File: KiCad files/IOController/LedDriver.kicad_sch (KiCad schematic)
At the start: 28 parts, among them IC1 TPS922054DMTR

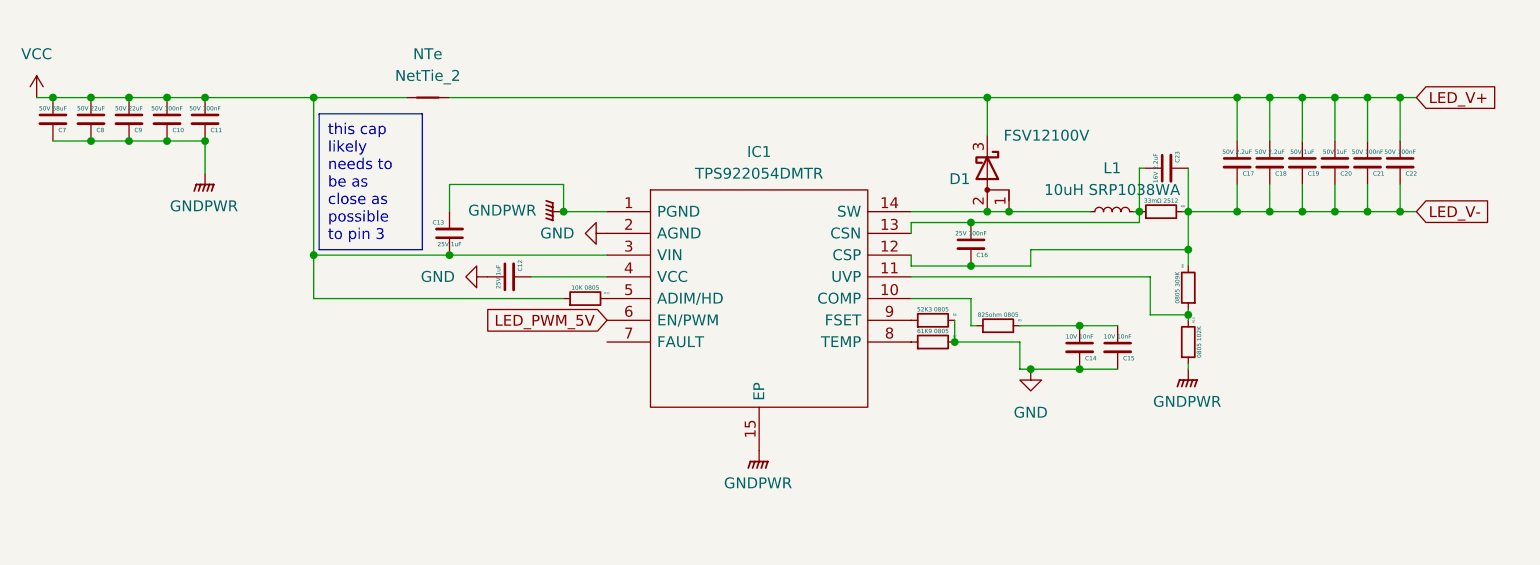
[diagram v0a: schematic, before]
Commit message: started re-work of led driver circuit on IO board
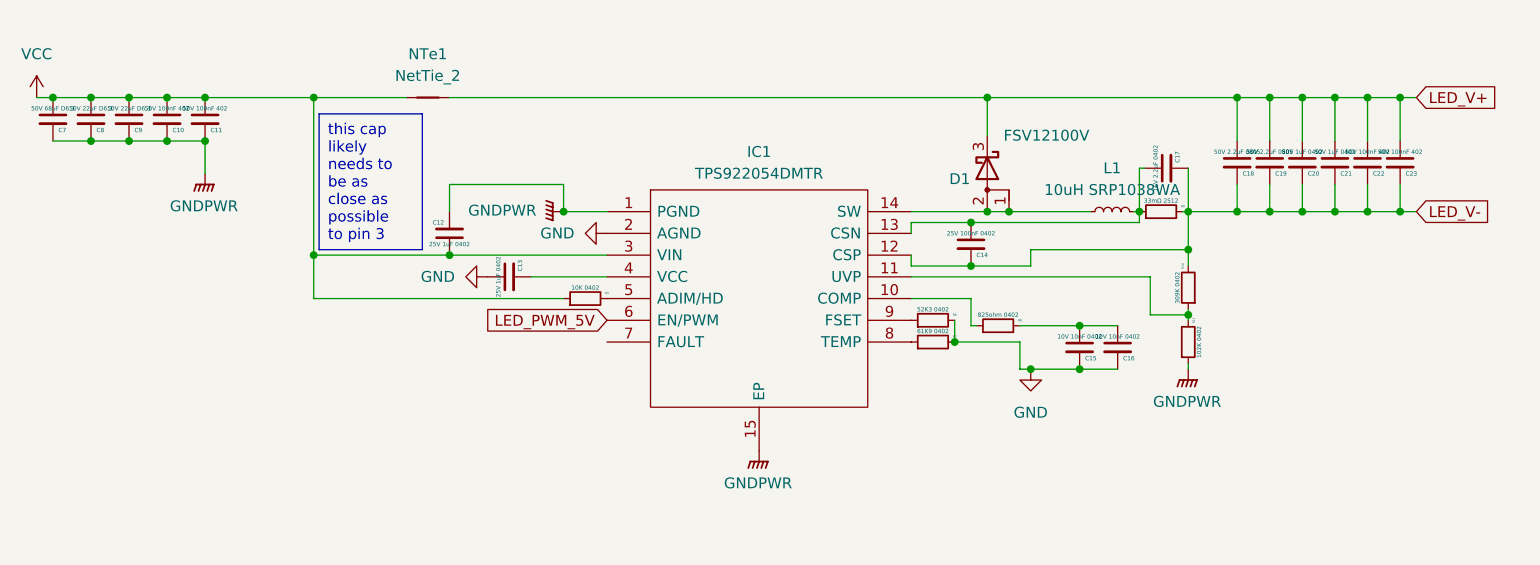
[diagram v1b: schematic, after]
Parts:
- C10, C11: value 50V 100nF -> 50V 100nF 402; footprint Capacitor_SMD:CP_Elec_8x5.4 -> Capacitor_SMD:C_0402_1005Metric
- C12: renamed from C13; value 25V 1uF -> 25V 1uF 0402; footprint Capacitor_SMD:CP_Elec_8x5.4 -> Capacitor_SMD:C_0402_1005Metric
- C13: renamed from C12; value 25V 1uF -> 25V 1uF 0402; footprint Capacitor_SMD:CP_Elec_8x5.4 -> Capacitor_SMD:C_0402_1005Metric
- C14: renamed from C16; value 25V 100nF -> 25V 100nF 0402; footprint Capacitor_SMD:CP_Elec_8x5.4 -> Capacitor_SMD:C_0402_1005Metric
- C15: renamed from C14; value 10V 10nF -> 10V 10nF 0402; footprint Capacitor_SMD:CP_Elec_8x5.4 -> Capacitor_SMD:C_0402_1005Metric
- C16: renamed from C15; value 10V 10nF -> 10V 10nF 0402; footprint Capacitor_SMD:CP_Elec_8x5.4 -> Capacitor_SMD:C_0402_1005Metric
- C17: renamed from C23; value 16V 2.2uF -> 16V 2.2uF 0402; footprint Capacitor_SMD:CP_Elec_8x5.4 -> Capacitor_SMD:C_0402_1005Metric
- C18: renamed from C17; value 50V 2.2uF -> 50V 2.2uF 0805; footprint Capacitor_SMD:CP_Elec_8x5.4 -> Capacitor_SMD:C_0805_2012Metric
- C19: renamed from C18; value 50V 2.2uF -> 50V 2.2uF 0805; footprint Capacitor_SMD:CP_Elec_8x5.4 -> Capacitor_SMD:C_0805_2012Metric
- C20: renamed from C19; value 50V 1uF -> 50V 1uF 0402; footprint Capacitor_SMD:CP_Elec_8x5.4 -> Capacitor_SMD:C_0402_1005Metric
- C21: renamed from C20; value 50V 1uF -> 50V 1uF 0402; footprint Capacitor_SMD:CP_Elec_8x5.4 -> Capacitor_SMD:C_0402_1005Metric
- C22: renamed from C21; value 50V 100nF -> 50V 100nF 402; footprint Capacitor_SMD:CP_Elec_8x5.4 -> Capacitor_SMD:C_0402_1005Metric
- C23: renamed from C22; value 50V 100nF -> 50V 100nF 402; footprint Capacitor_SMD:CP_Elec_8x5.4 -> Capacitor_SMD:C_0402_1005Metric
- C7: value 50V 68uF -> 50V 68uF D6.3; footprint Capacitor_SMD:CP_Elec_8x5.4 -> Capacitor_SMD:CP_Elec_6.3x5.9
- C8, C9: value 50V 22uF -> 50V 22uF D6.3; footprint Capacitor_SMD:CP_Elec_8x5.4 -> Capacitor_SMD:CP_Elec_6.3x5.9
- R10: renamed from R9; value 0805 309K -> 309K 0402; footprint Resistor_SMD:R_0805_2012Metric -> Resistor_SMD:R_0402_1005Metric
- R11: renamed from R10; value 0805 102K -> 102K 0402; footprint Resistor_SMD:R_0805_2012Metric -> Resistor_SMD:R_0402_1005Metric
- R5: renamed from R11; value 10K 0805 -> 10K 0402; footprint Resistor_SMD:R_0805_2012Metric -> Resistor_SMD:R_0402_1005Metric
- R6: value 52K3 0805 -> 52K3 0402; footprint Resistor_SMD:R_0805_2012Metric -> Resistor_SMD:R_0402_1005Metric
- R7: value 61K9 0805 -> 61K9 0402; footprint Resistor_SMD:R_0805_2012Metric -> Resistor_SMD:R_0402_1005Metric
- R8: renamed from R5; value 825ohm 0805 -> 825ohm 0402; footprint Resistor_SMD:R_0805_2012Metric -> Resistor_SMD:R_0402_1005Metric
- renumbered NTe to NTe1, R8 to R9

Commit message: completed circuit, could be laid out better
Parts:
- removed NTe1: NetTie_2, NetTie:NetTie-2_THT_Pad1.0mm, symbol Device:NetTie_2
- C8, C9: value 50V 22uF D6.3 -> 35V 22uF 1206; footprint Capacitor_SMD:CP_Elec_6.3x5.9 -> Capacitor_SMD:C_1206_3216Metric
- L1: value 10uH SRP1038WA -> VLS6045AF-100M; footprint Inductor_SMD:L_Bourns_SRP1038C_10.0x10.0mm -> Inductor_SMD:L_TDK_VLS6045EX_VLS6045AF
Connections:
- net GNDPWR is gone; now on net GND: C10.2, C11.2, C12.2, C7.2, C8.2, C9.2, IC1.1 (PGND), IC1.15 (EP), R11.1
- net LED_V+ is gone; now on net VCC: C18.1, C19.1, C20.1, C21.1, C22.1, C23.1, D1.3 (K)

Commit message: laid out the circuit better but less space efficient.
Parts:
- C10, C11, C22, C23: value 50V 100nF 402 -> 50V 100nF 0805; footprint Capacitor_SMD:C_0402_1005Metric -> Capacitor_SMD:C_0805_2012Metric
- C20, C21: value 50V 1uF 0402 -> 50V 1uF 0805; footprint Capacitor_SMD:C_0402_1005Metric -> Capacitor_SMD:C_0805_2012Metric
- C7: value 50V 68uF D6.3 -> 35V 68uF; footprint Capacitor_SMD:CP_Elec_6.3x5.9 -> Capacitor_Tantalum_SMD:CP_EIA-7343-43_Kemet-X
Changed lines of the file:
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@@
       (effects (font (size 0.5 0.5)) (justify left))
     )
-    (property "Value" "50V 100nF 402" (at 176.53 52.07 0)
-      (effects (font (size 0.5 0.5)))
-    )
-    (property "Footprint" "Capacitor_SMD:C_0402_1005Metric" (at 176.53 53.34 0)
+    (property "Value" "50V 100nF 0805" (at 176.53 52.07 0)
+      (effects (font (size 0.5 0.5)))
+    )
+    (property "Footprint" "Capacitor_SMD:C_0805_2012Metric" (at 176.53 53.34 0)
       (effects (font (size 1.27 1.27)) hide)
     )
@@
       (effects (font (size 0.5 0.5)) (justify left))
     )
-    (property "Value" "50V 100nF 402" (at 40.64 46.99 0)
-      (effects (font (size 0.5 0.5)))
-    )
-    (property "Footprint" "Capacitor_SMD:C_0402_1005Metric" (at 40.64 48.26 0)
+    (property "Value" "50V 100nF 0805" (at 40.64 46.99 0)
+      (effects (font (size 0.5 0.5)))
+    )
+    (property "Footprint" "Capacitor_SMD:C_0805_2012Metric" (at 40.64 48.26 0)
       (effects (font (size 1.27 1.27)) hide)
     )
@@
       (effects (font (size 0.5 0.5)) (justify left))
     )
-    (property "Value" "50V 100nF 402" (at 180.34 52.07 0)
-      (effects (font (size 0.5 0.5)))
-    )
-    (property "Footprint" "Capacitor_SMD:C_0402_1005Metric" (at 180.34 53.34 0)
+    (property "Value" "50V 100nF 0805" (at 180.34 52.07 0)
+      (effects (font (size 0.5 0.5)))
+    )
+    (property "Footprint" "Capacitor_SMD:C_0805_2012Metric" (at 180.34 53.34 0)
       (effects (font (size 1.27 1.27)) hide)
     )
@@
       (effects (font (size 0.5 0.5)) (justify left))
     )
-    (property "Value" "50V 1uF 0402" (at 172.72 52.07 0)
-      (effects (font (size 0.5 0.5)))
-    )
-    (property "Footprint" "Capacitor_SMD:C_0402_1005Metric" (at 172.72 53.34 0)
+    (property "Value" "50V 1uF 0805" (at 172.72 52.07 0)
+      (effects (font (size 0.5 0.5)) hide)
+    )
+    (property "Footprint" "Capacitor_SMD:C_0805_2012Metric" (at 172.72 53.34 0)
       (effects (font (size 1.27 1.27)) hide)
     )
@@
       (effects (font (size 0.5 0.5)) (justify left))
     )
-    (property "Value" "50V 68uF D6.3" (at 22.86 46.99 0)
-      (effects (font (size 0.5 0.5)))
-    )
-    (property "Footprint" "Capacitor_SMD:CP_Elec_6.3x5.9" (at 22.86 48.26 0)
+    (property "Value" "35V 68uF" (at 22.86 46.99 0)
+      (effects (font (size 0.5 0.5)))
+    )
+    (property "Footprint" "Capacitor_Tantalum_SMD:CP_EIA-7343-43_Kemet-X" (at 22.86 48.26 0)
       (effects (font (size 1.27 1.27)) hide)
     )
@@
       (effects (font (size 0.5 0.5)) (justify left))
     )
-    (property "Value" "50V 100nF 402" (at 36.195 46.99 0)
-      (effects (font (size 0.5 0.5)))
-    )
-    (property "Footprint" "Capacitor_SMD:C_0402_1005Metric" (at 36.195 48.26 0)
+    (property "Value" "50V 100nF 0805" (at 36.195 46.99 0)
+      (effects (font (size 0.5 0.5)))
+    )
+    (property "Footprint" "Capacitor_SMD:C_0805_2012Metric" (at 36.195 48.26 0)
       (effects (font (size 1.27 1.27)) hide)
     )
@@
       (effects (font (size 0.5 0.5)) (justify left))
     )
-    (property "Value" "50V 1uF 0402" (at 168.91 52.07 0)
-      (effects (font (size 0.5 0.5)))
-    )
-    (property "Footprint" "Capacitor_SMD:C_0402_1005Metric" (at 168.91 53.34 0)
-      (effects (font (size 1.27 1.27)) hide)
-    )
+    (property "Value" "50V 1uF 0805" (at 168.91 52.07 0)
+      (effects (font (size 0.5 0.5)))
+    )
+    (property "Footprint" "Capacitor_SMD:C_0805_2012Metric" (at 168.91 53.34 0)
+      (effects (font (size 1.27 1.27)) hide)
+    )

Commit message: updated small changes
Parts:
- added NT1: NetTie, NetTie:NetTie-2_SMD_Pad2.0mm, symbol Device:NetTie_2
- added R12, R13: 0Ω 0402, Resistor_SMD:R_0402_1005Metric, symbol Device:R_Small
- C14: value 25V 100nF 0402 -> 50V 0.1uF 0805; footprint Capacitor_SMD:C_0402_1005Metric -> Capacitor_SMD:C_0805_2012Metric
- C17: value 16V 2.2uF 0402 -> Csense 50V 2.2uF 0805; footprint Capacitor_SMD:C_0402_1005Metric -> Capacitor_SMD:C_0805_2012Metric
- IC1: value TPS922054DMTR -> TPS923654DMTR
- L1: value VLS6045AF-100M -> SRP1770TA-220M; footprint Inductor_SMD:L_TDK_VLS6045EX_VLS6045AF -> Inductor_SMD:L_Bourns_SRP1770TA_16.9x16.9mm
- R10: value 309K 0402 -> Rovp1 232K 0402
- R11: value 102K 0402 -> Rovp2 10K 0402
- R6: value 52K3 0402 -> Rfset 52K3 0402
- R7: value 61K9 0402 -> Rtemp 61K9 0402
- R8: value 825ohm 0402 -> Rcomp 825ohm 0402
- R9: value 33mΩ 2512 -> Rsense 65mΩ 2512
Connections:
- net GND: now also NT1.1
- net LED_V-: now also NT1.2; no longer C14.2, C17.2, IC1.12 (CSP), R10.2, R9.2
- net VCC: now also L1.1; no longer C18.1, C19.1, C20.1, C21.1, C22.1, C23.1, D1.3 (K)
- net at C14.1, C17.1, R9.1: now also D1.3 (K), R12.2; no longer IC1.13 (CSN), L1.2
- net at D1.1 (A), D1.2 (A), IC1.14 (SW): now also L1.2; no longer L1.1
- new net: IC1.12 (CSP), R13.1
- new net: IC1.13 (CSN), R12.1
- new net LED V+: C14.2, C17.2, C18.1, C19.1, C20.1, C21.1, C22.1, C23.1, R10.2, R13.2, R9.2
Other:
- moved on the sheet: C10, C11, C15, C16, C17, C18, C19, C20, C21, C22, C23, C7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

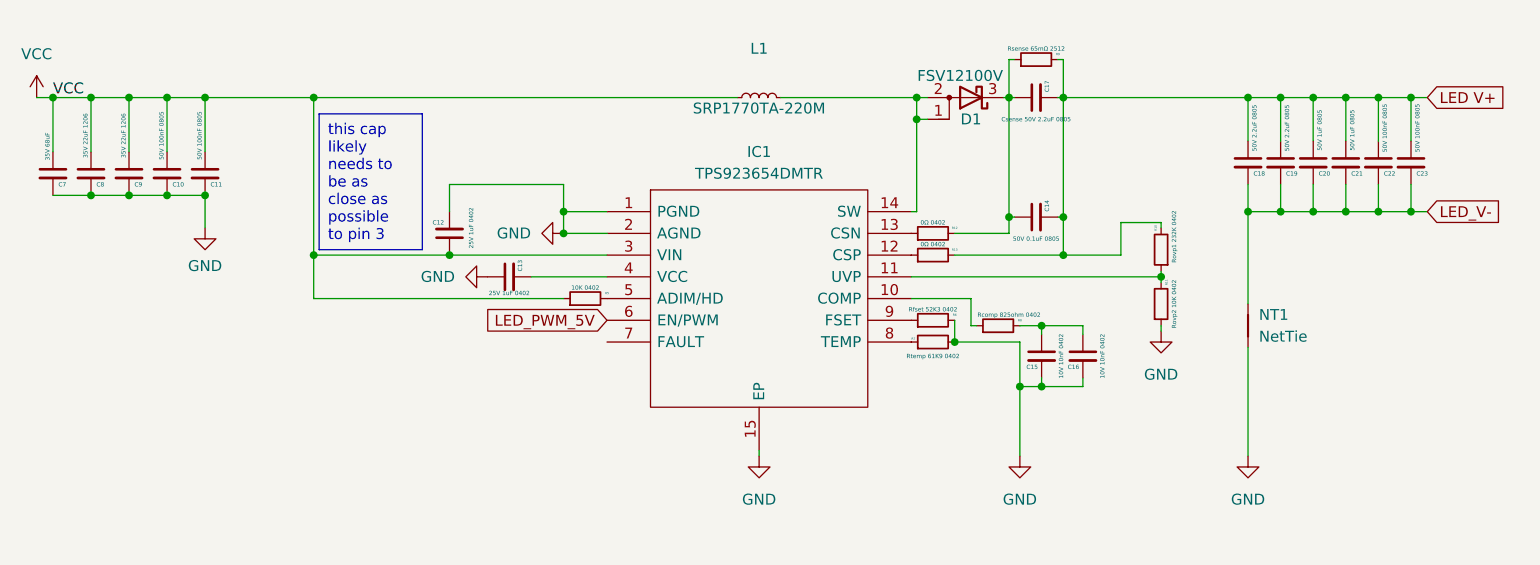
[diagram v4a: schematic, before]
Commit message: re-organised some files, started work on implementing 100W and 240W EPR versions of the charge board
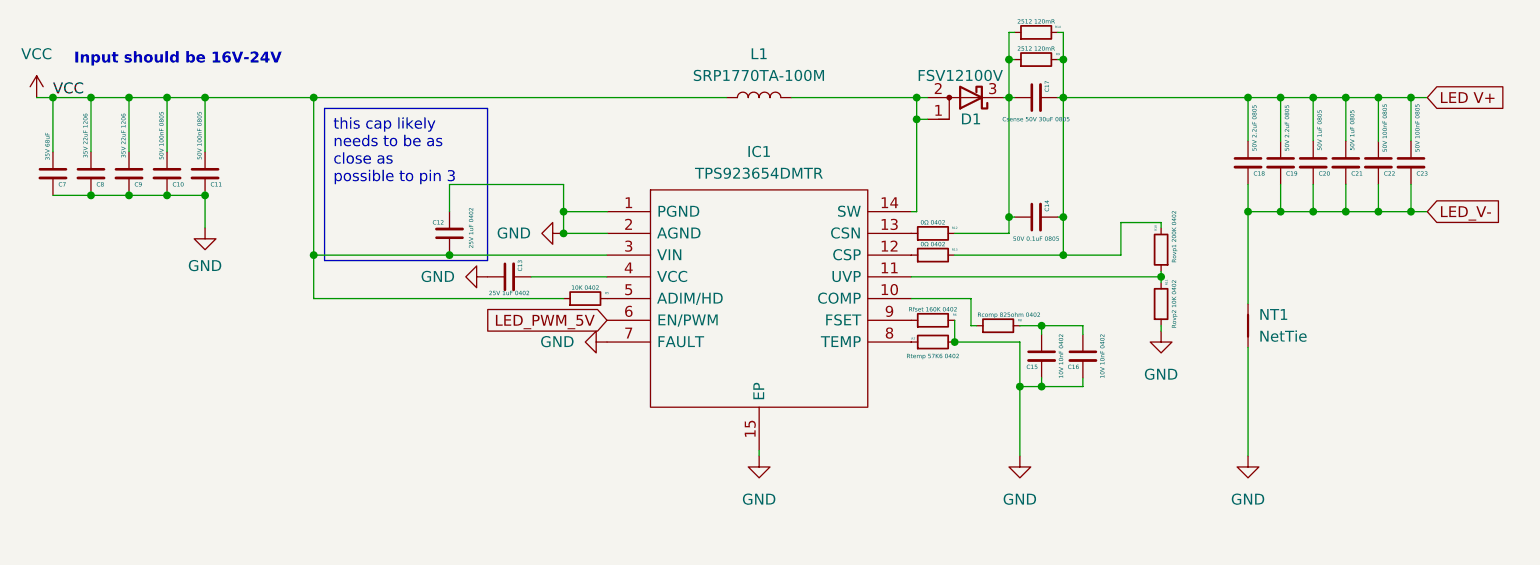
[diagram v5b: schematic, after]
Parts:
- removed L1: SRP1770TA-220M, Inductor_SMD:L_Bourns_SRP1770TA_16.9x16.9mm, symbol Device:L_Small
- added L1: SRP1770TA-100M, Inductor_SMD:L_Bourns_SRP1770TA_16.9x16.9mm, symbol Device:L
- added R14: 2512 120mR, Resistor_SMD:R_2512_6332Metric, symbol Device:R_Small
- C17: value Csense 50V 2.2uF 0805 -> Csense 50V 30uF 0805
- R10: value Rovp1 232K 0402 -> Rovp1 200K 0402
- R6: value Rfset 52K3 0402 -> Rfset 160K 0402
- R7: value Rtemp 61K9 0402 -> Rtemp 57K6 0402
- R9: value Rsense 65mΩ 2512 -> 2512 120mR
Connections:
- net GND: now also IC1.7 (FAULT)
- net LED V+: now also R14.2
- net VCC: now also L1.1
- net at D1.1 (A), D1.2 (A), IC1.14 (SW): now also L1.2
- net at C14.1, C17.1, D1.3 (K)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: now also R14.1
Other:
- note added: "Input should be 16V-24V"

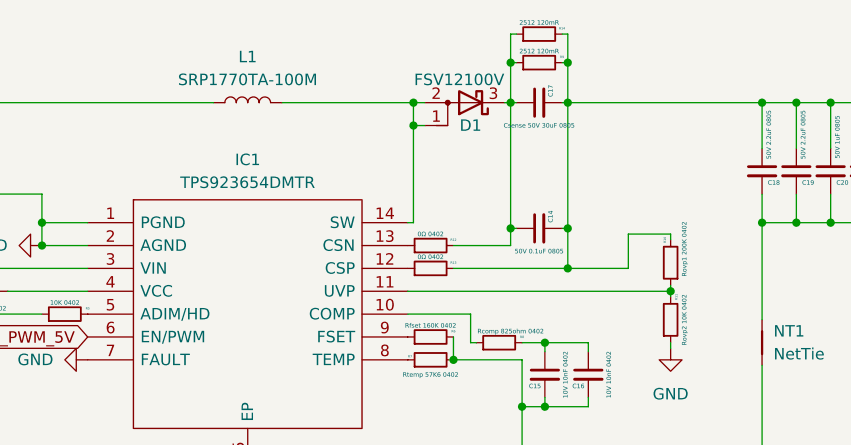
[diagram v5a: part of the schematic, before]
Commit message: made some adjustments to improve design reliability.
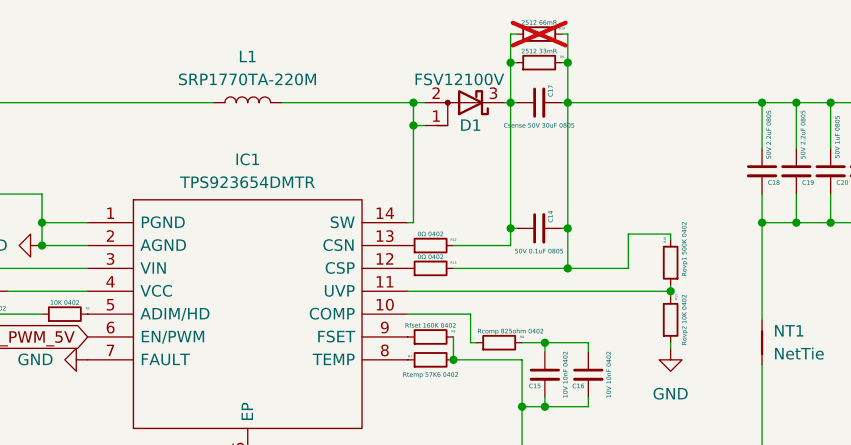
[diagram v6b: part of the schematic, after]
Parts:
- L1: value SRP1770TA-100M -> SRP1770TA-220M
- R10: value Rovp1 200K 0402 -> Rovp1 500K 0402
- R14: value 2512 120mR -> 2512 66mR; now not fitted; now left out of the parts list
- R9: value 2512 120mR -> 2512 33mR
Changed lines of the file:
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@@
 		(unit 1)
 		(exclude_from_sim no)
-		(in_bom yes)
-		(on_board yes)
-		(dnp no)
+		(in_bom no)
+		(on_board yes)
+		(dnp yes)
 		(property "Reference" "R14"
 			(at 140.335 37.465 90)
@@
 			)
 		)
-		(property "Value" "2512 120mR"
+		(property "Value" "2512 66mR"
 			(at 137.795 36.83 90)
 			(effects
@@
 			)
 		)
-		(property "Value" "SRP1770TA-100M"
+		(property "Value" "SRP1770TA-220M"
 			(at 105.41 43.18 90)
 			(effects
@@
 			)
 		)
-		(property "Value" "2512 120mR"
+		(property "Value" "2512 33mR"
 			(at 137.795 40.005 90)
 			(effects
@@
 			)
 		)
-		(property "Value" "Rovp1 200K 0402"
+		(property "Value" "Rovp1 500K 0402"
 			(at 153.924 61.976 90)
 			(effects
